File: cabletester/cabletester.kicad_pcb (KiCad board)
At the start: 2 copper layers, 131 x 64 mm, 25 parts, among them J1 IDC 2x5, J2 IDC 2x8, J3 IDC 2x5, J4 IDC 2x8, J5 OLED, U1 4051

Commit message: Gerbers, update PCB, updated README
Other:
- board size 131 x 64 mm -> 131 x 50.5 mm

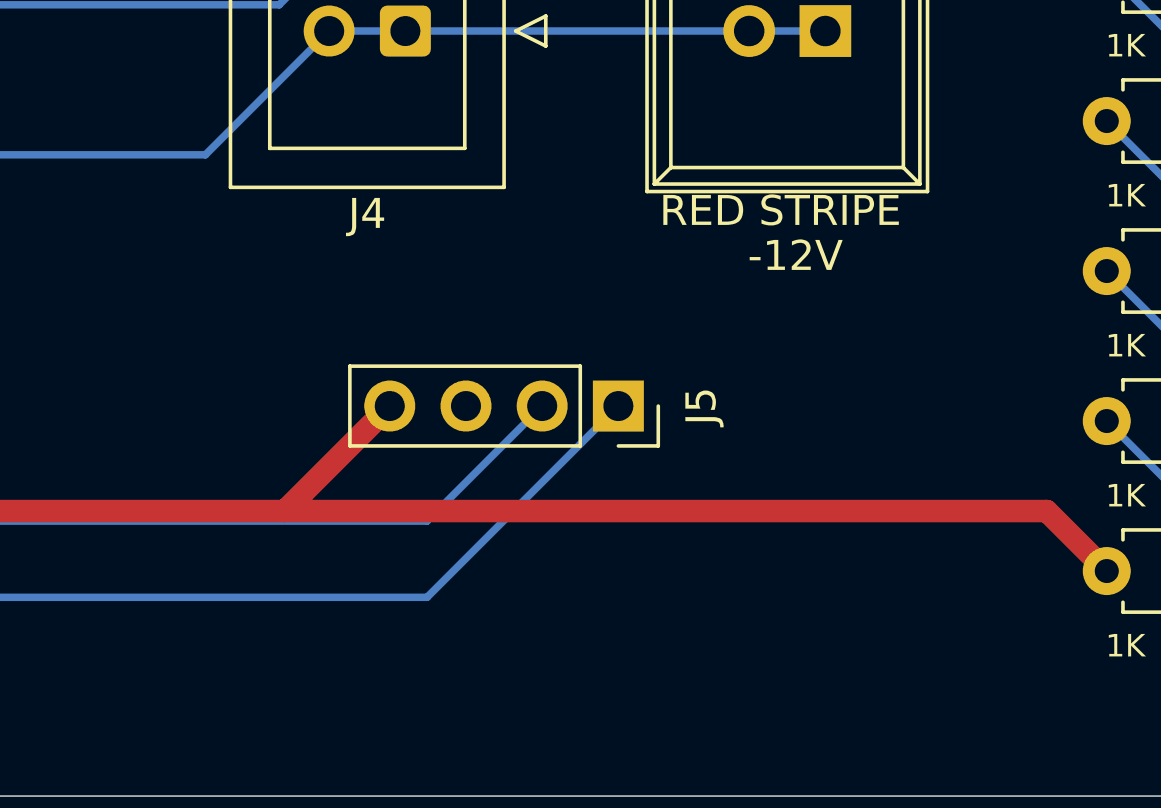
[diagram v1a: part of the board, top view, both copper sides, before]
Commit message: Add 2nd header for alternate OLED pinout
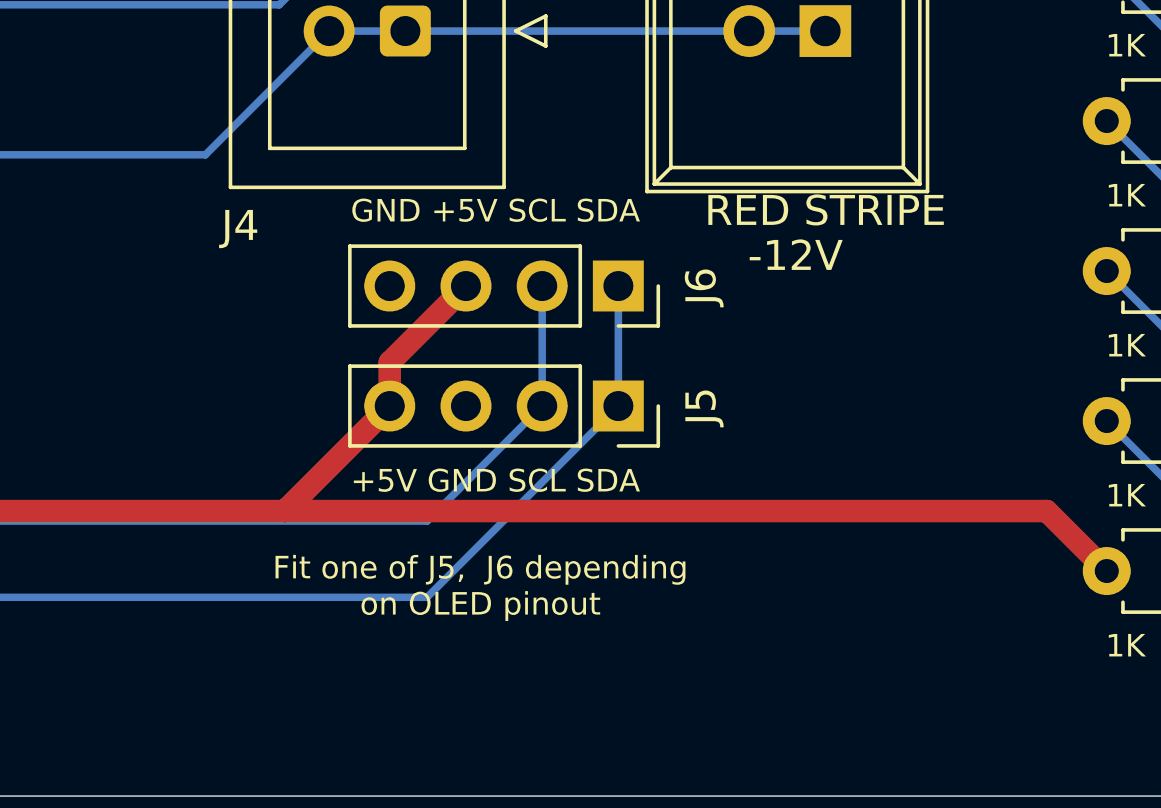
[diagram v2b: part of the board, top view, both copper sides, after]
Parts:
- added J6: OLED, Connector_PinSocket_2.54mm:PinSocket_1x04_P2.54mm_Vertical, F.Cu at (137.1, 67.5)
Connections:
- net /S0 renamed S0
- net /S1 renamed S1
- net /S2 renamed S2
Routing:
- net +5V: track 102.3 -> 107.4 mm
- net A5: track 72.2 -> 76.2 mm
- net A4: track 85.7 -> 89.7 mm
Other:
- board text added: "+5V GND SCL SDA"
- board text added: "Fit one of J5, J6 depending on OLED pinout"
- board text added: "GND +5V SCL SDA"

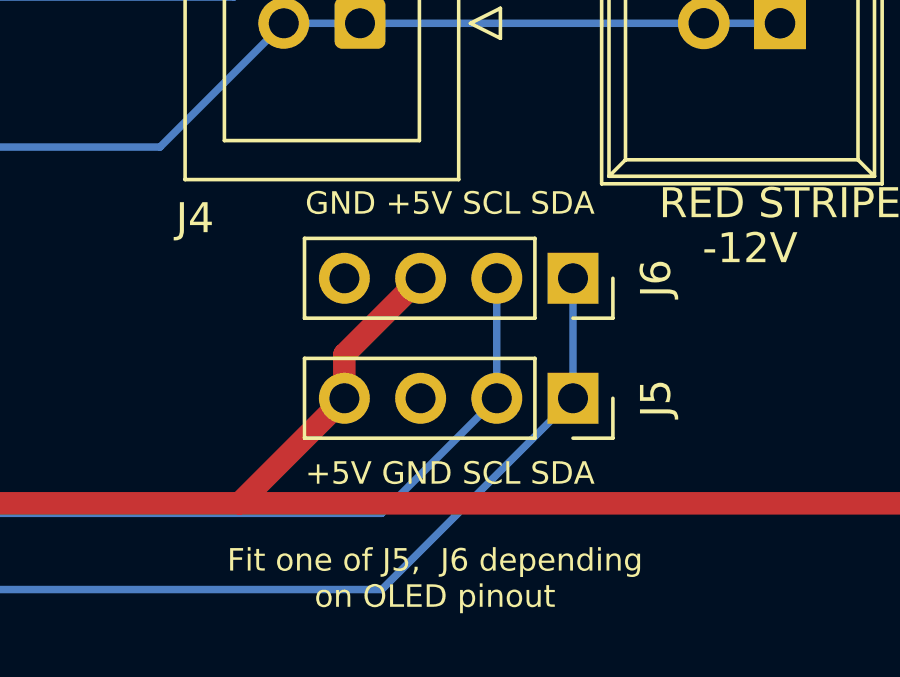
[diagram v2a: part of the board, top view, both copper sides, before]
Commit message: README update for OLED info, show PCB; change label on PCB
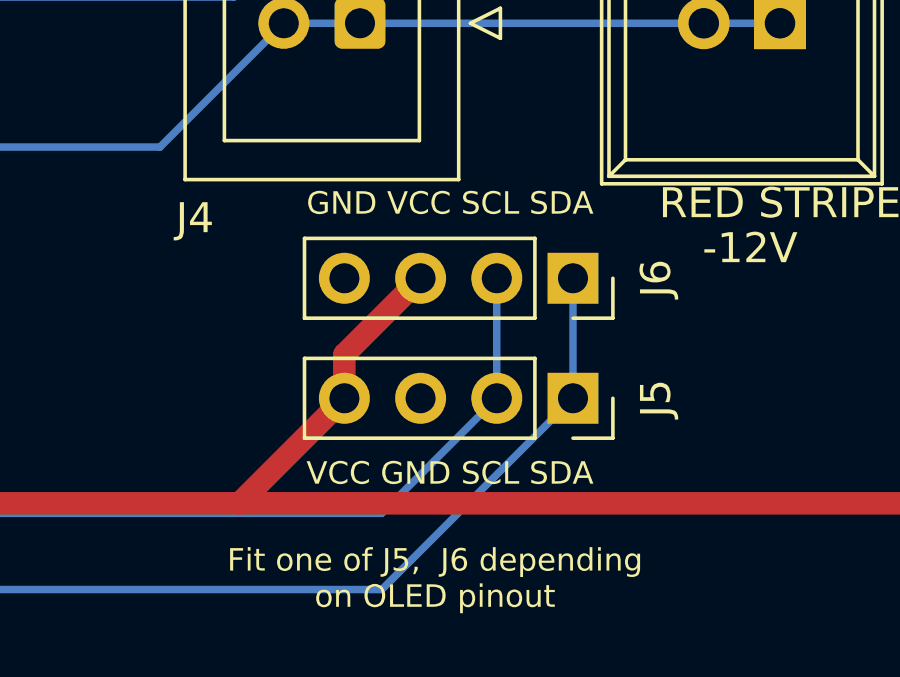
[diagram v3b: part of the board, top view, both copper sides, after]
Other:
- board text added: "GND VCC SCL SDA"
- board text added: "VCC GND SCL SDA"
- board text removed: "+5V GND SCL SDA"
- board text removed: "GND +5V SCL SDA"

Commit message: BOM; change header label
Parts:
- J5, J6: value OLED -> 4 pin header
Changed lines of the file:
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@@
       (effects (font (size 1 1) (thickness 0.15)))
     )
-    (fp_text value OLED (at 0 10.39 90) (layer F.Fab)
+    (fp_text value "4 pin header" (at 0 10.39 90) (layer F.Fab)
       (effects (font (size 1 1) (thickness 0.15)))
     )
@@
       (effects (font (size 1 1) (thickness 0.15)))
     )
-    (fp_text value OLED (at 0 10.39 90) (layer F.Fab)
-      (effects (font (size 1 1) (thickness 0.15)))
-    )
+    (fp_text value "4 pin header" (at 0 10.39 90) (layer F.Fab)
+      (effects (font (size 1 1) (thickness 0.15)))
+    )

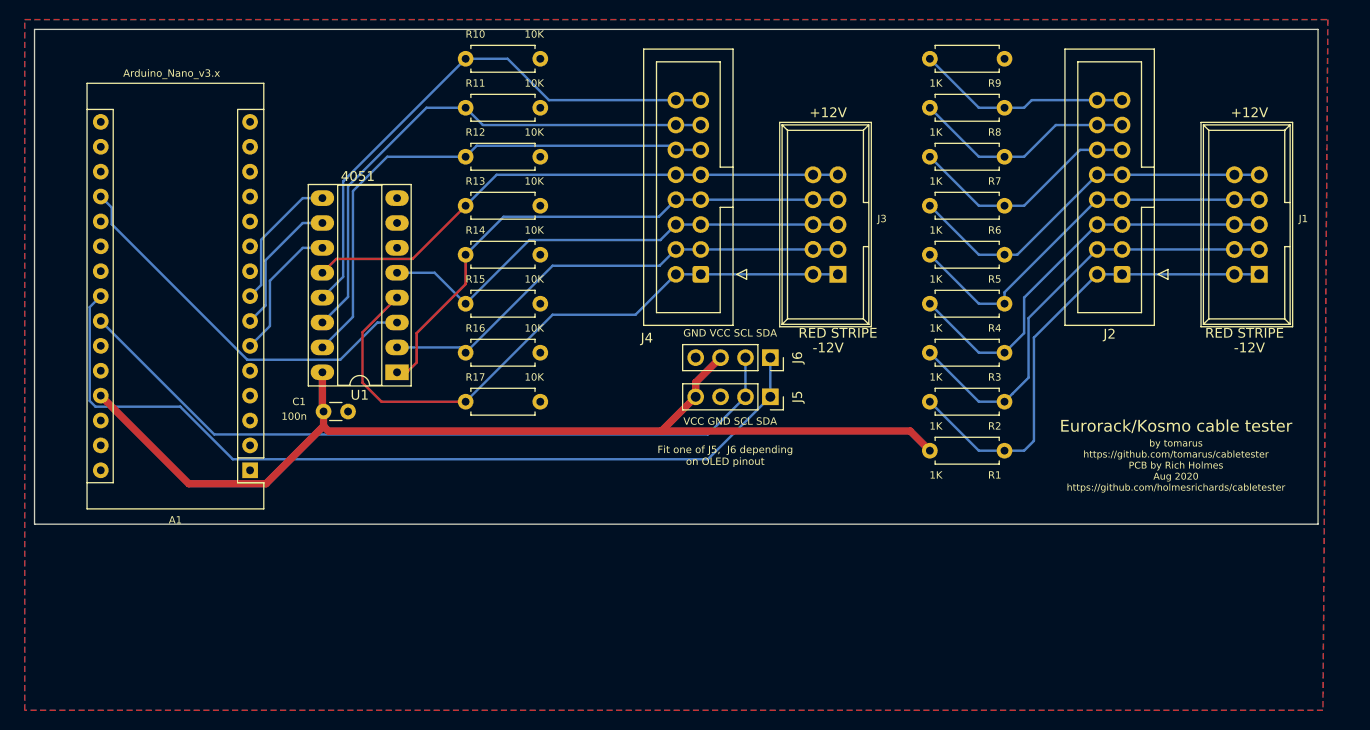
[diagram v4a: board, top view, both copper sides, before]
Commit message: added mounting holes, new Gerbers
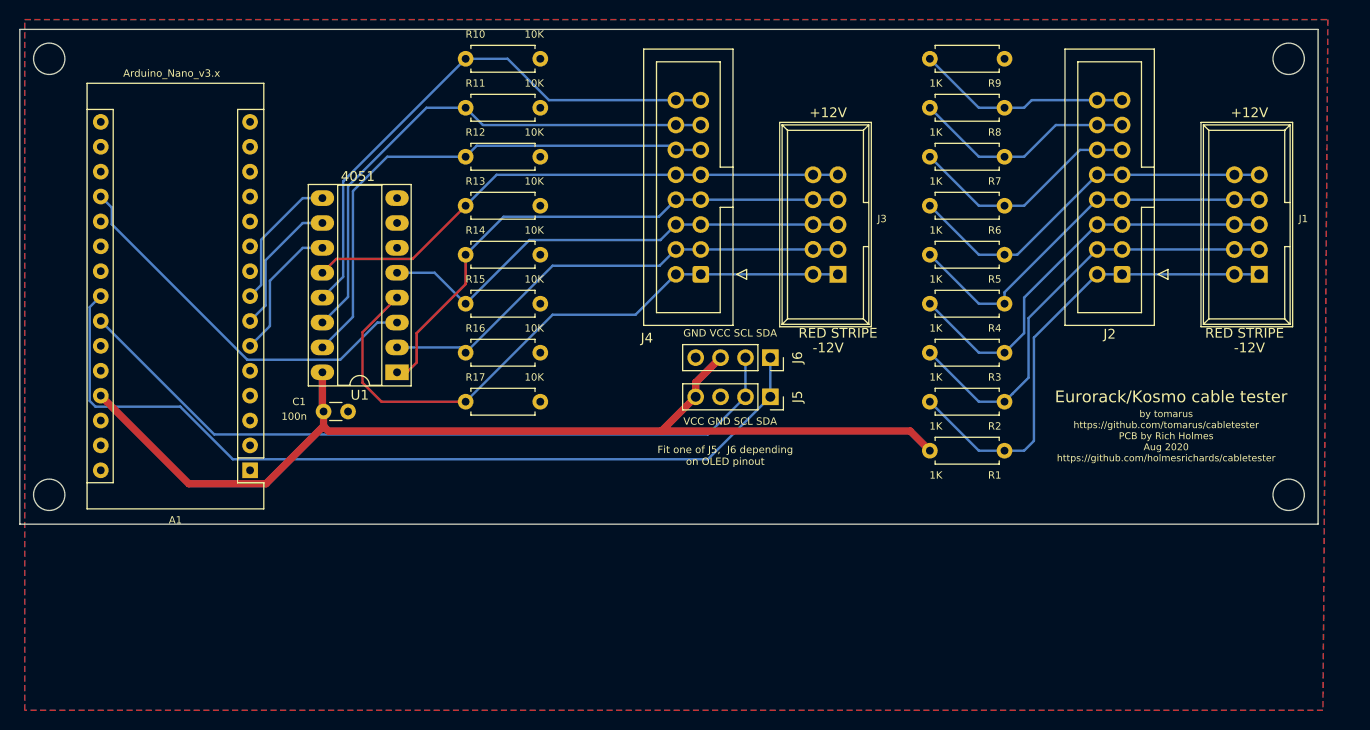
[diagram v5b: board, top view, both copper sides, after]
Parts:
- added REF**: MountingHole_3.2mm_M3, ao_tht:MountingHole_3.2mm_M3, F.Cu at (63.5, 37.0)
- added REF**: MountingHole_3.2mm_M3, ao_tht:MountingHole_3.2mm_M3, F.Cu at (63.5, 81.5)
- added REF**: MountingHole_3.2mm_M3, ao_tht:MountingHole_3.2mm_M3, F.Cu at (190.0, 81.5)
- added REF**: MountingHole_3.2mm_M3, ao_tht:MountingHole_3.2mm_M3, F.Cu at (190.0, 37.0)
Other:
- board size 131 x 50.5 mm -> 132.5 x 50.5 mm
